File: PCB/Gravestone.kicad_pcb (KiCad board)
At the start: 2 copper layers, 60 x 40 mm, 31 parts, among them J1 USB_C_Receptacle_USB2.0, SW1 SW_PUSH, U1 ATmega32U4-AU, Y1 16MHz

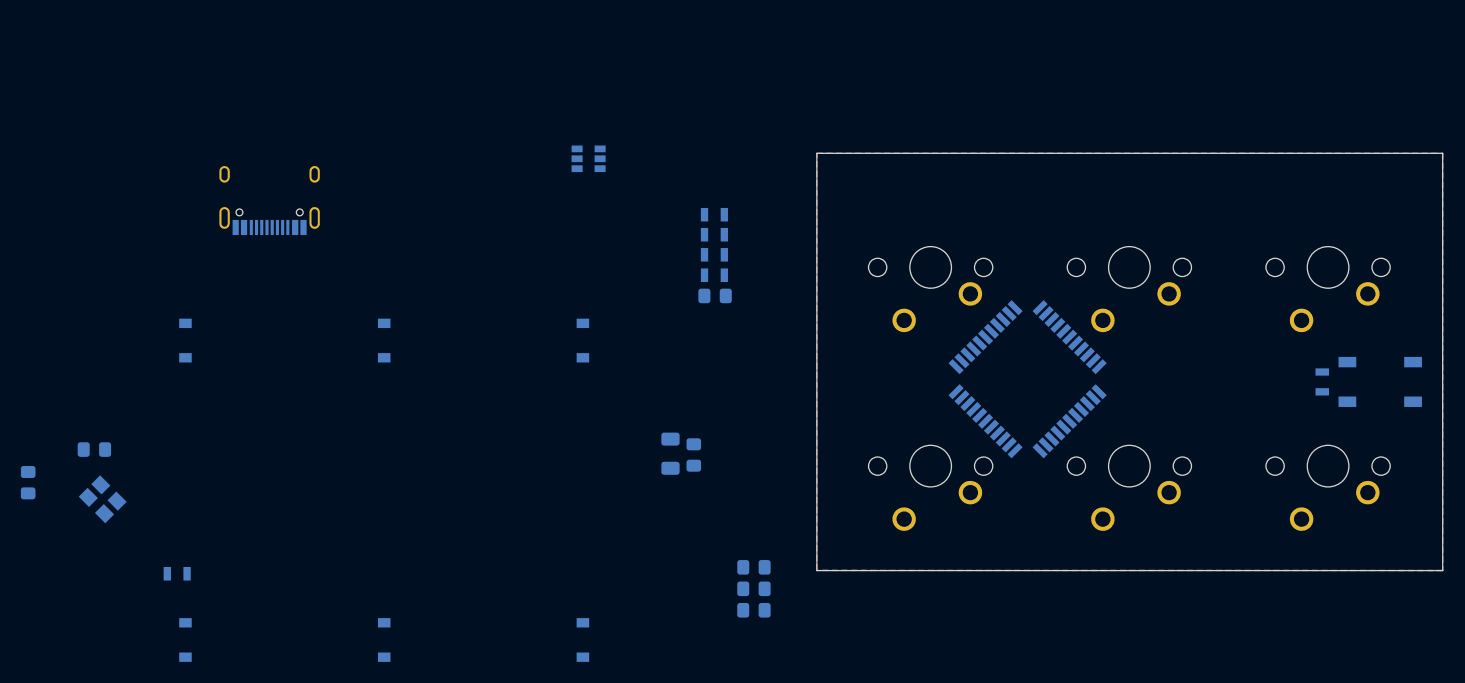
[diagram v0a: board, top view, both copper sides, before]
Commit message: swapped 32u4 for 32u2 to save space
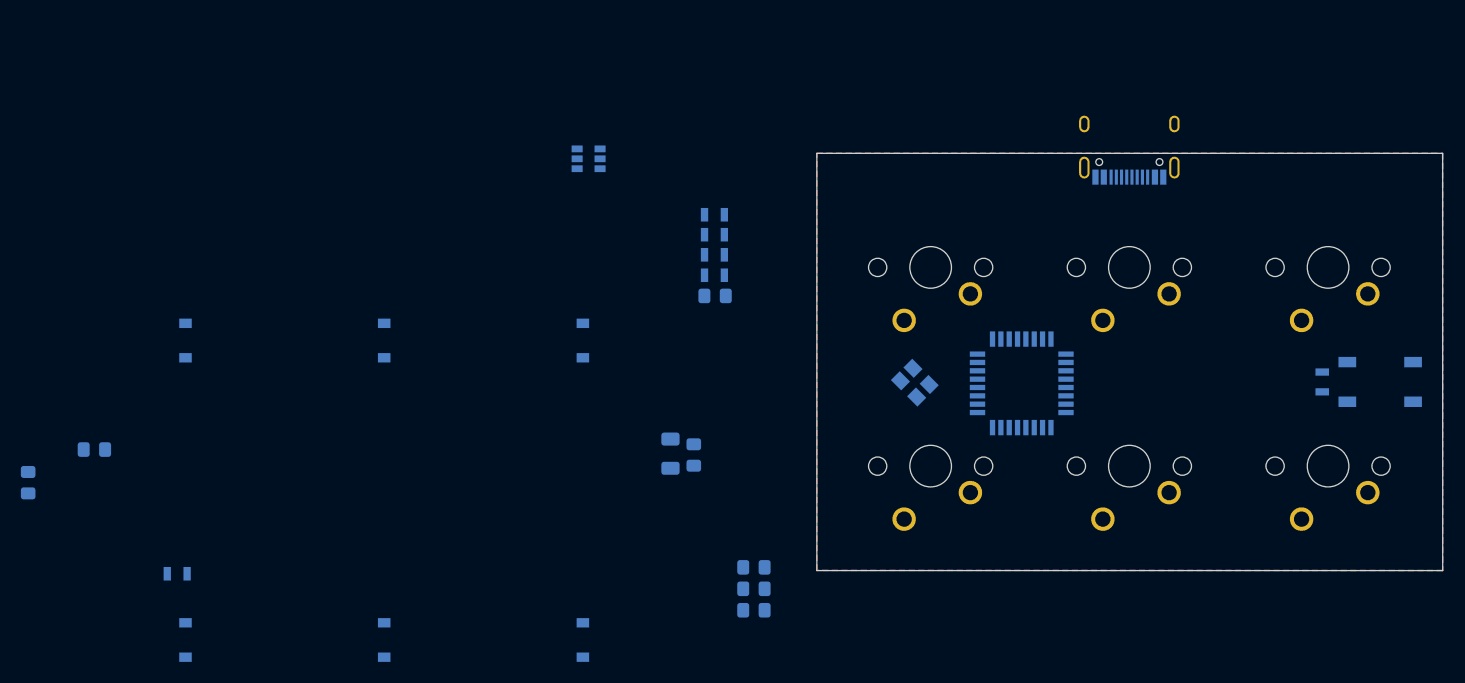
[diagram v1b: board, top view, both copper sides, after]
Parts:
- removed U1: ATmega32U4-AU, Package_QFP:TQFP-44_10x10mm_P0.8mm
- added Ue: ATmega32U2-AU, 32u2:ATMEGA32U2-AU, B.Cu at (142.1, 100.0)
- moved J1 82.6 mm to (152.4, 76.2)
- moved Y1 78.7 mm to (131.8, 99.9), turned to 135 degrees

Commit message: 9/07
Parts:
- removed C3: 0.1uF, Capacitor_SMD:C_0805_2012Metric_Pad1.15x1.40mm_HandSolder
- C1, C2, C4, C5, C7: footprint Capacitor_SMD:C_0805_2012Metric_Pad1.15x1.40mm_HandSolder -> Capacitor_SMD:C_0603_1608Metric_Pad1.05x0.95mm_HandSolder
- C6: value 10uF -> 4.7uF; footprint Capacitor_SMD:C_0805_2012Metric_Pad1.15x1.40mm_HandSolder -> Capacitor_SMD:C_0603_1608Metric_Pad1.05x0.95mm_HandSolder
- F1: footprint Fuse:Fuse_1206_3216Metric -> Fuse:Fuse_0805_2012Metric
- J1: footprint Connector_USB:USB_C_Receptacle_HRO_TYPE-C-31-M-12 -> usb-type-c:Mid_Mount-USB_C_HandSoldering; moved to F.Cu
- R1, R2, R3, R4, R5, R7: footprint Keebio-Parts:R_0805 -> Keebio-Parts:R_0603
- moved R7 70.6 mm to (119.9, 79.2), turned to 90 degrees
- moved D5 56.6 mm to (104.9, 87.7), turned to 0 degrees
- moved D6 47.9 mm to (111.3, 87.6), turned to 0 degrees
- moved C4 41.5 mm to (83.7, 94.1)
- moved D7 40.7 mm to (117.5, 87.8), turned to 0 degrees
- moved C5 38.7 mm to (89.5, 93.9)
- moved C6 27.1 mm to (84.6, 99.6), turned to 0 degrees
- moved C1 25.4 mm to (67.1, 94.1), turned to 180 degrees
- moved D2 24.7 mm to (85.2, 87.7), turned to 0 degrees
- moved C7 24.2 mm to (89.9, 99.7), turned to 0 degrees
- moved D1 23.7 mm to (78.4, 86.7)
- moved C2 22.5 mm to (72.2, 94.3)
- moved F1 14.6 mm to (100.6, 94.4)
- moved D3 13.4 mm to (91.4, 87.4), turned to 180 degrees
- moved R2 12.1 mm to (104.1, 79.1), turned to 90 degrees
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- renumbered Ue to U1
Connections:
- net Net-(U1-Pad10) renamed ROW2
- U1 pad 6: Net-(U1-Pad6) -> COL0
- U1 pad 7: Net-(U1-Pad7) -> COL1
- U1 pad 8: Net-(U1-Pad8) -> COL2
- U1 pad 9: Net-(U1-Pad9) -> ROW0
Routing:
- removed copper zone on B.Cu, net GND
- removed copper zone on F.Cu, net GND

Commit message: 9/7 usb
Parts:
- J1: value USB_C_Receptacle_USB2.0 -> USB2_C_Receptacle
- moved J1 6.54 mm to (152.4, 71.7)
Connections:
- J1 pad A1B12: (no net) -> GND
- J1 pad A4B9: (no net) -> VBUS
- J1 pad A6: D- -> D+
- J1 pad A7: D+ -> D-
- J1 pad B1A12: (no net) -> GND
- J1 pad B4A9: (no net) -> VBUS
- J1 pad B6: D- -> D+
- J1 pad B7: D+ -> D-
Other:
- board size 60 x 40 mm -> 60 x 46.3 mm

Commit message: 9/07 usb2
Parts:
- J1: moved to B.Cu
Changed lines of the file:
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@@
     (add_net VBUS)
   )
-  (module usb-type-c:Mid_Mount-USB_C_HandSoldering (layer F.Cu)
+  (module usb-type-c:Mid_Mount-USB_C_HandSoldering (layer B.Cu)
     (at 152.4 71.66864 90)
-    (fp_text reference J1 (at -1.27 -7.62 90) (layer F.SilkS)
-      (effects (font (size 0.8 0.8) (thickness 0.15)))
+    (fp_text reference J1 (at -1.27 7.62 270) (layer B.SilkS)
+      (effects (font (size 0.8 0.8) (thickness 0.15)) (justify mirror))
     )
-    (fp_text value USB2_C_Receptacle (at 0 8.89 90) (layer F.Fab)
-      (effects (font (size 1 1) (thickness 0.15)))
+    (fp_text value USB2_C_Receptacle (at 0 -8.89 270) (layer B.Fab)
+      (effects (font (size 1 1) (thickness 0.15)) (justify mirror))
     )
+    (fp_arc (start -6.43 3.75) (end -5.6 3.75) (angle -60) (layer Edge.Cuts) (width 0.15))
     (fp_arc (start -6.43 -3.75) (end -5.6 -3.75) (angle 60) (layer Edge.Cuts) (width 0.15))
-    (fp_arc (start -6.43 3.75) (end -5.6 3.75) (angle -60) (layer Edge.Cuts) (width 0.15))
+    (fp_arc (start -5.6 4.37) (end -5.6 4.67) (angle 150) (layer Edge.Cuts) (width 0.15))
+    (fp_arc (start -5.9 3.850384) (end -5.6 3.850384) (angle 60) (layer Edge.Cuts) (width 0.15))
+    (fp_arc (start -5.73 2.537565) (end -6.3 2.537565) (angle -60) (layer Edge.Cuts) (width 0.15))
+    (fp_arc (start -5.73 -2.537565) (end -6.3 -2.537565) (angle 60) (layer Edge.Cuts) (width 0.15))
+    (fp_arc (start -5.9 -3.850384) (end -5.6 -3.850384) (angle -60) (layer Edge.Cuts) (width 0.15))
     (fp_arc (start -5.6 -4.37) (end -5.6 -4.67) (angle -150) (layer Edge.Cuts) (width 0.15))
-    (fp_arc (start -5.9 -3.850384) (end -5.6 -3.850384) (angle -60) (layer Edge.Cuts) (width 0.15))
-    (fp_arc (start -5.73 -2.537565) (end -6.3 -2.537565) (angle 60) (layer Edge.Cuts) (width 0.15))
-    (fp_arc (start -5.73 2.537565) (end -6.3 2.537565) (angle -60) (layer Edge.Cuts) (width 0.15))
-    (fp_arc (start -5.9 3.850384) (end -5.6 3.850384) (angle 60) (layer Edge.Cuts) (width 0.15))
-    (fp_arc (start -5.6 4.37) (end -5.6 4.67) (angle 150) (layer Edge.Cuts) (width 0.15))
-    (fp_line (start 0 6.35) (end 0 -6.35) (layer F.CrtYd) (width 0.05))
-    (fp_line (start -9.05 4.699) (end -7.747 4.699) (layer F.CrtYd) (width 0.05))
-    (fp_line (start -9.05 -4.7) (end -9.05 4.698) (layer F.CrtYd) (width 0.05))
-    (fp_line (start -7.747 -4.699) (end -9.05 -4.699) (layer F.CrtYd) (width 0.05))
-    (fp_line (start -7.747 -6.35) (end -7.747 -4.699) (layer F.CrtYd) (width 0.05))
-    (fp_line (start 0 -6.35) (end -7.747 -6.35) (layer F.CrtYd) (width 0.05))
-    (fp_line (start -7.747 6.35) (end -7.747 4.699) (layer F.CrtYd) (width 0.05))
-    (fp_line (start 0 6.35) (end -7.747 6.35) (layer F.CrtYd) (width 0.05))
+    (fp_line (start 0 -6.35) (end 0 6.35) (layer B.CrtYd) (width 0.05))
+    (fp_line (start -9.05 -4.699) (end -7.747 -4.699) (layer B.CrtYd) (width 0.05))
+    (fp_line (start -9.05 4.7) (end -9.05 -4.698) (layer B.CrtYd) (width 0.05))
+    (fp_line (start -7.747 4.699) (end -9.05 4.699) (layer B.CrtYd) (width 0.05))
+    (fp_line (start -7.747 6.35) (end -7.747 4.699) (layer B.CrtYd) (width 0.05))
+    (fp_line (start 0 6.35) (end -7.747 6.35) (layer B.CrtYd) (width 0.05))
+    (fp_line (start -7.747 -6.35) (end -7.747 -4.699) (layer B.CrtYd) (width 0.05))
+    (fp_line (start 0 -6.35) (end -7.747 -6.35) (layer B.CrtYd) (width 0.05))
+    (fp_line (start -5.6 3.850384) (end -5.6 3.75) (layer Edge.Cuts) (width 0.15))
+    (fp_line (start -6.3 -2.537566) (end -6.3 2.537566) (layer Edge.Cuts) (width 0.15))
+    (fp_line (start -0.3 6.5) (end -9.2 6.5) (layer B.SilkS) (width 0.15))
+    (fp_line (start -9.2 6.5) (end -9.2 -6.5) (layer B.SilkS) (width 0.15))
+    (fp_line (start -9.2 -6.5) (end -0.3 -6.5) (layer B.SilkS) (width 0.15))
+    (fp_line (start 0 -7.62) (end 0 -4.67) (layer Edge.Cuts) (width 0.15))
+    (fp_line (start 0 -4.67) (end -5.6 -4.67) (layer Edge.Cuts) (width 0.15))
     (fp_line (start -5.6 -3.850384) (end -5.6 -3.75) (layer Edge.Cuts) (width 0.15))
-    (fp_line (start -6.3 2.537566) (end -6.3 -2.537566) (layer Edge.Cuts) (width 0.15))
-    (fp_line (start -0.3 -6.5) (end -9.2 -6.5) (layer F.SilkS) (width 0.15))
-    (fp_line (start -9.2 -6.5) (end -9.2 6.5) (layer F.SilkS) (width 0.15))
-    (fp_line (start -9.2 6.5) (end -0.3 6.5) (layer F.SilkS) (width 0.15))
-    (fp_line (start 0 7.62) (end 0 4.67) (layer Edge.Cuts) (width 0.15))
-    (fp_line (start 0 4.67) (end -5.6 4.67) (layer Edge.Cuts) (width 0.15))
-    (fp_line (start -5.6 3.850384) (end -5.6 3.75) (layer Edge.Cuts) (width 0.15))
-    (fp_line (start -5.6 -4.67) (end 0 -4.67) (layer Edge.Cuts) (width 0.15))
-    (fp_line (start 0 -4.67) (end 0 -7.62) (layer Edge.Cuts) (width 0.15))
-    (pad S1 smd rect (at -1.75 5.2 180) (size 0.7 2.3) (layers F.Cu F.Mask)
+    (fp_line (start -5.6 4.67) (end 0 4.67) (layer Edge.Cuts) (width 0.15))
+    (fp_line (start 0 4.67) (end 0 7.62) (layer Edge.Cuts) (width 0.15))
+    (pad S1 smd rect (at -1.75 -5.2) (size 0.7 2.3) (layers B.Cu B.Mask)
       (net 33 GND) (zone_connect 2))
-    (pad S1 smd rect (at -1.75 -5.2 180) (size 0.7 2.3) (layers F.Cu F.Mask)
+    (pad S1 smd rect (at -1.75 5.2) (size 0.7 2.3) (layers B.Cu B.Mask)
       (net 33 GND) (zone_connect 2))
-    (pad S1 thru_hole oval (at -6.35 5.575 180) (size 1.2 2.3) (drill oval 0.5 1.65) (layers *.Cu *.Mask)
+    (pad S1 thru_hole oval (at -6.35 -5.575) (size 1.2 2.3) (drill oval 0.5 1.65) (layers *.Cu *.Mask)
       (net 33 GND))
-    (pad S1 thru_hole oval (at -6.35 -5.575 180) (size 1.2 2.3) (drill oval 0.5 1.65) (layers *.Cu *.Mask)
+    (pad S1 thru_hole oval (at -6.35 5.575) (size 1.2 2.3) (drill oval 0.5 1.65) (layers *.Cu *.Mask)
       (net 33 GND))
-    (pad S1 thru_hole oval (at -1.75 5.575 180) (size 1.2 2.3) (drill oval 0.5 1.65) (layers *.Cu *.Mask)
+    (pad S1 thru_hole oval (at -1.75 -5.575) (size 1.2 2.3) (drill oval 0.5 1.65) (layers *.Cu *.Mask)
       (net 33 GND))
-    (pad S1 thru_hole oval (at -1.75 -5.575 180) (size 1.2 2.3) (drill oval 0.5 1.65) (layers *.Cu *.Mask)
+    (pad S1 thru_hole oval (at -1.75 5.575) (size 1.2 2.3) (drill oval 0.5 1.65) (layers *.Cu *.Mask)
       (net 33 GND))
-    (pad "" np_thru_hole circle (at -6.43 3.75 180) (size 0.6 0.6) (drill 0.4) (layers *.Cu *.Mask))
-    (pad "" np_thru_hole circle (at -6.43 -3.75 180) (size 0.6 0.6) (drill 0.4) (layers *.Cu *.Mask))
-    (pad A1B12 smd rect (at -7.93 3.2 180) (size 0.55 1.7) (layers F.Cu F.Paste F.Mask)
+    (pad "" np_thru_hole circle (at -6.43 -3.75) (size 0.6 0.6) (drill 0.4) (layers *.Cu *.Mask))
+    (pad "" np_thru_hole circle (at -6.43 3.75) (size 0.6 0.6) (drill 0.4) (layers *.Cu *.Mask))
+    (pad A1B12 smd rect (at -7.93 -3.2) (size 0.55 1.7) (layers B.Cu B.Paste B.Mask)
       (net 33 GND))
-    (pad B1A12 smd rect (at -7.93 -3.2 180) (size 0.55 1.7) (layers F.Cu F.Paste F.Mask)
+    (pad B1A12 smd rect (at -7.93 3.2) (size 0.55 1.7) (layers B.Cu B.Paste B.Mask)
       (net 33 GND))
-    (pad A4B9 smd rect (at -7.93 2.45 180) (size 0.55 1.7) (layers F.Cu F.Paste F.Mask)
+    (pad A4B9 smd rect (at -7.93 -2.45) (size 0.55 1.7) (layers B.Cu B.Paste B.Mask)
       (net 35 VBUS))
-    (pad B8 smd rect (at -7.93 1.75 180) (size 0.3 1.7) (layers F.Cu F.Paste F.Mask)
+    (pad B8 smd rect (at -7.93 -1.75) (size 0.3 1.7) (layers B.Cu B.Paste B.Mask)
       (net 38 "Net-(J1-PadB8)"))
-    (pad A5 smd rect (at -7.93 1.25 180) (size 0.3 1.7) (layers F.Cu F.Paste F.Mask)
+    (pad A5 smd rect (at -7.93 -1.25) (size 0.3 1.7) (layers B.Cu B.Paste B.Mask)
       (net 19 "Net-(J1-PadA5)"))
-    (pad B7 smd rect (at -7.93 0.75 180) (size 0.3 1.7) (layers F.Cu F.Paste F.Mask)
+    (pad B7 smd rect (at -7.93 -0.75) (size 0.3 1.7) (layers B.Cu B.Paste B.Mask)
       (net 7 D-))
-    (pad B4A9 smd rect (at -7.93 -2.45 180) (size 0.55 1.7) (layers F.Cu F.Paste F.Mask)
+    (pad B4A9 smd rect (at -7.93 2.45) (size 0.55 1.7) (layers B.Cu B.Paste B.Mask)
       (net 35 VBUS))
-    (pad B5 smd rect (at -7.93 -1.75 180) (size 0.3 1.7) (layers F.Cu F.Paste F.Mask)
+    (pad B5 smd rect (at -7.93 1.75) (size 0.3 1.7) (layers B.Cu B.Paste B.Mask)
       (net 20 "Net-(J1-PadB5)"))
-    (pad A8 smd rect (at -7.93 -1.25 180) (size 0.3 1.7) (layers F.Cu F.Paste F.Mask)
+    (pad A8 smd rect (at -7.93 1.25) (size 0.3 1.7) (layers B.Cu B.Paste B.Mask)
       (net 37 "Net-(J1-PadA8)"))
-    (pad B6 smd rect (at -7.93 -0.75 180) (size 0.3 1.7) (layers F.Cu F.Paste F.Mask)
+    (pad B6 smd rect (at -7.93 0.75) (size 0.3 1.7) (layers B.Cu B.Paste B.Mask)
       (net 6 D+))
-    (pad A7 smd rect (at -7.93 -0.25 180) (size 0.3 1.7) (layers F.Cu F.Paste F.Mask)
+    (pad A7 smd rect (at -7.93 0.25) (size 0.3 1.7) (layers B.Cu B.Paste B.Mask)
       (net 7 D-))
-    (pad A6 smd rect (at -7.93 0.25 180) (size 0.3 1.7) (layers F.Cu F.Paste F.Mask)
+    (pad A6 smd rect (at -7.93 -0.25) (size 0.3 1.7) (layers B.Cu B.Paste B.Mask)
       (net 6 D+))
   )

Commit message: 9/7 1021
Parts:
- moved D1 78.2 mm to (156.6, 85.6), turned to 0 degrees
- moved D3 69.8 mm to (160.6, 95.8), turned to 270 degrees
- moved D4 65.9 mm to (163.2, 95.9), turned to 270 degrees
- moved C1 63.3 mm to (129.9, 101.6), turned to 135 degrees
- moved C2 61.8 mm to (133.8, 98.4), turned to 315 degrees
- moved F1 57.2 mm to (156.6, 82.7), turned to 0 degrees
- moved D6 56.3 mm to (160.7, 114.7), turned to 270 degrees
- moved C7 55.1 mm to (144.4, 107.4), turned to 270 degrees
- moved R3 53.6 mm to (161.1, 84.4), turned to 180 degrees
- moved D7 53.1 mm to (163.2, 114.7), turned to 270 degrees
- moved C4 50.9 mm to (134.1, 101.8), turned to 225 degrees
- moved C6 44.1 mm to (128.5, 103.9), turned to 180 degrees
- moved R2 43.1 mm to (146.8, 84.5), turned to 0 degrees
- moved R4 42.2 mm to (142.6, 107.3), turned to 270 degrees
- moved D2 40.8 mm to (125.3, 95.7), turned to 270 degrees
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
